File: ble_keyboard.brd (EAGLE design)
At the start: 52 x 23 mm, 18 parts, among them CN1 FH34SRJ-6S, CN2 FH34SRJ-10S, CON1 41002W90-NP-S-30, Q1 DMG6968U-7, U1 YJ-14015

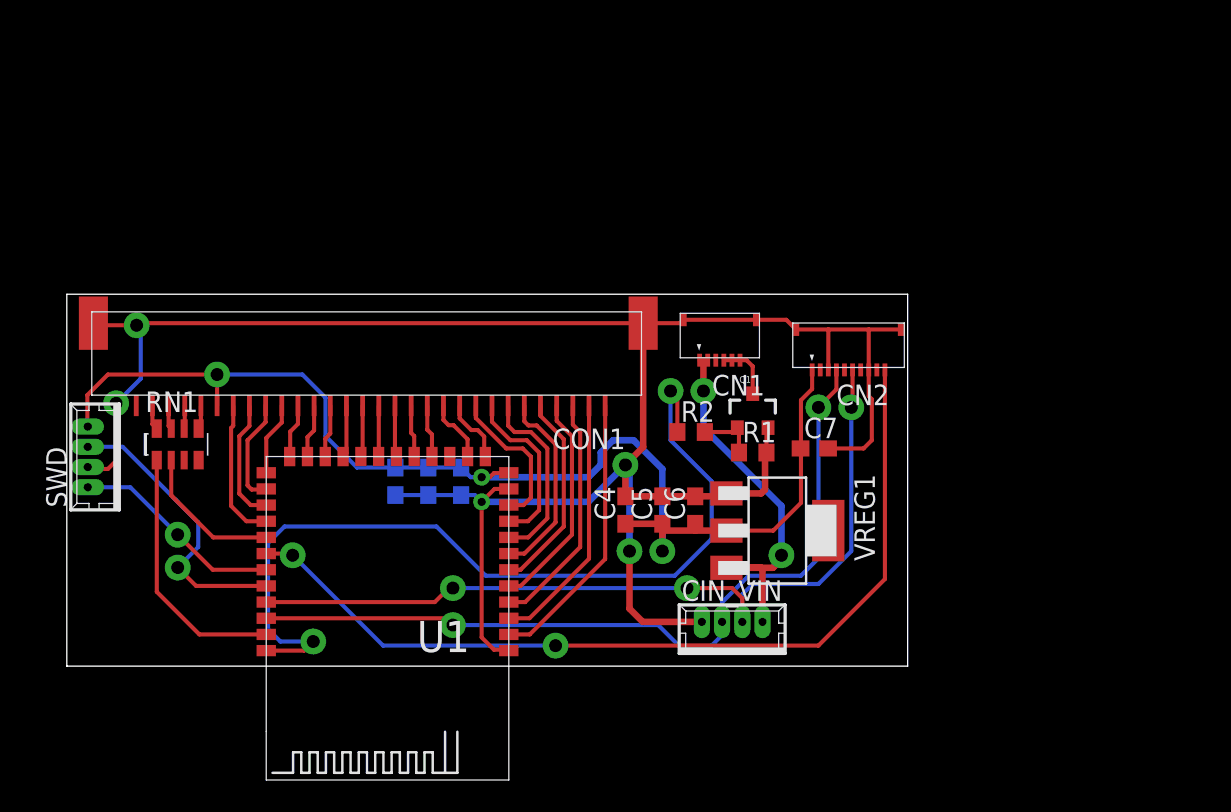
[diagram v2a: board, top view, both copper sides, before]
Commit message: Brd routed with 90 degree rotated BLE module, fixed touchpad and Keyboard pinout
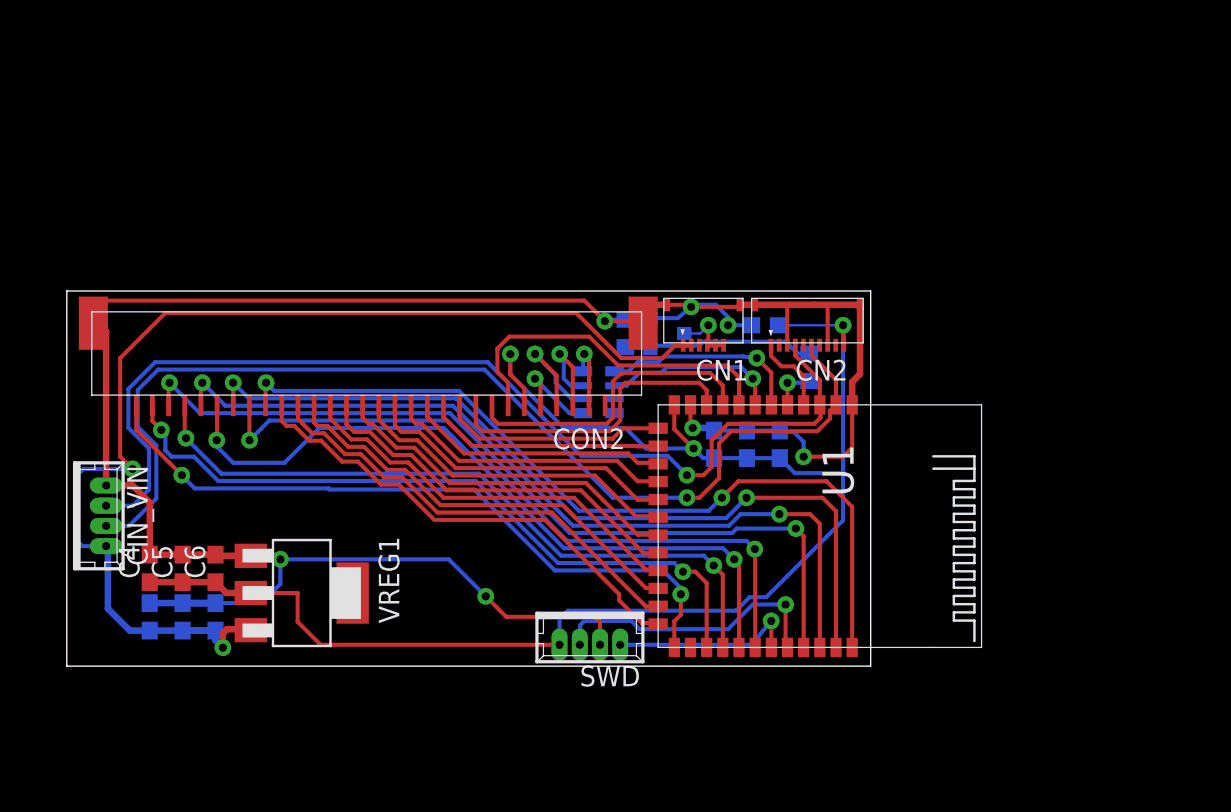
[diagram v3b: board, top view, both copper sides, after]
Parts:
- added C10: 1uF, rcl:C0603
- added C8: 10nF, rcl:C0603
- added C9: 100n, rcl:C0603
- moved CIN_VIN 39.8 mm to (1.98, 9.30), turned to 270 degrees
- moved SWD 32.6 mm to (32.4, 1.77), turned to 180 degrees
- moved C6 29.9 mm to (9.19, 6.05)
- moved C5 29.9 mm to (7.16, 6.05)
- moved VREG1 29.7 mm to (14.5, 4.52)
- moved C4 29.6 mm to (5.13, 6.05)
- moved RN1 26.2 mm to (32.9, 16.9), flipped to the bottom, turned to 270 degrees
- moved C3 23.9 mm to (44.1, 13.7), turned to 90 degrees
- moved C2 19.8 mm to (42.1, 13.7), turned to 90 degrees
- moved U1 17.3 mm to (36.6, 8.66), turned to 270 degrees
- moved C1 15.8 mm to (40.0, 13.7), turned to 90 degrees
- moved R1 10.8 mm to (34.5, 20.6), flipped to the bottom, turned to 90 degrees
- moved R2 8.33 mm to (45.9, 18.5), flipped to the bottom, turned to 90 degrees
- moved C7 8.21 mm to (43.2, 21.1), flipped to the bottom
- moved Q1 7.19 mm to (37.1, 20.6), flipped to the bottom, turned to 90 degrees
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- renumbered CON1 to CON2
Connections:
- net +3V3: now also CN2.10, CON2.6; no longer CN2.1, CON2.25
- net BACKLIGHT_PWM: now also U1.P.24; no longer U1.P.20
- net GND: now also C10.2, C8.2, C9.2
- net I2C_SCL: now also CIN_VIN.2, CN2.6, U1.P.21; no longer CIN_VIN.3, CN2.4, U1.P.18
- net I2C_SDA: now also CIN_VIN.3, CN2.4, U1.P.22; no longer CIN_VIN.2, CN2.6, U1.P.17
- net KSI0: now also CON2.25, U1.P.15; no longer CON2.5, U1.P.25
- net KSI1: now also CON2.23, U1.P.16; no longer CON2.7, U1.P.27
- net KSI2: now also CON2.24, U1.P.19; no longer CON2.8, U1.P.28
- net KSI3: now also CON2.22, U1.P.20; no longer CON2.9, U1.P.29
- net KSI4: now also CON2.21, U1.P.10; no longer CON2.10, U1.P.30
- net KSI5: now also CON2.19, U1.P.08; no longer CON2.12, U1.P.02
- net KSI6: now also CON2.17, U1.P.06; no longer CON2.14, U1.P.04
- net KSI7: now also CON2.16; no longer CON2.15
- net KSO0: now also CON2.30, U1.P.11; no longer CON2.1, U1.P.21
- net KSO1: now also CON2.29, U1.P.13; no longer CON2.2, U1.P.22
- net KSO10: now also CON2.12, U1.P.01; no longer CON2.19, U1.P.09
- net KSO11: now also CON2.11, U1.P.00; no longer CON2.20, U1.P.10
- net KSO12: now also CON2.10, U1.P.30; no longer CON2.21, U1.P.11
- net KSO13: now also CON2.9, U1.P.29; no longer CON2.22, U1.P.12
- net KSO14: now also CON2.8, U1.P.28; no longer CON2.23, U1.P.13
- net KSO15: now also CON2.7, U1.P.27; no longer CON2.24, U1.P.14
- net KSO2: now also CON2.27, U1.P.14; no longer CON2.3, U1.P.23
- net KSO3: now also CON2.28, U1.P.17; no longer CON2.4, U1.P.24
- net KSO4: now also CON2.26, U1.P.18; no longer CON2.6, U1.P.26
- net KSO5: now also CON2.20, U1.P.09; no longer CON2.11, U1.P.00
- net KSO6: now also CON2.18, U1.P.07; no longer CON2.13, U1.P.03
- net KSO7: now also CON2.15, U1.P.04; no longer CON2.16, U1.P.06
- net KSO8: now also CON2.14, U1.P.03; no longer CON2.17, U1.P.07
- net KSO9: now also CON2.13, U1.P.02; no longer CON2.18, U1.P.08
- net LED_CAPS: now also U1.P.26; no longer U1.P.15
- net LED_FN: now also U1.P.25; no longer U1.P.19
- net LIPO_RAW: now also C10.1, C8.1, C9.1
- net N$1: now also CON2.5; no longer CON2.26
- net N$2: now also CON2.4; no longer CON2.27
- net N$3: now also CON2.3; no longer CON2.28
- net N$4: now also CON2.2; no longer CON2.29
- net TOUCH_ALERT: now also CN2.1, U1.P.23; no longer CN2.10, U1.P.16
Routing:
- net BACKLIGHT_PWM: track 54.6 -> 2.75 mm, vias 2 -> 1
- net TOUCH_ALERT: track 55.3 -> 4.97 mm, vias 2 -> 0
- net LIPO_RAW: track 24.0 -> 72.0 mm
- net KSI3: track 9.26 -> 51.1 mm, vias 0 -> 2
- net KSI2: track 10.4 -> 51.5 mm, vias 0 -> 2
- net KSO4: track 12.0 -> 51.5 mm, vias 0 -> 2
- net KSO3: track 13.6 -> 51.7 mm, vias 0 -> 2
- net KSI0: track 12.6 -> 44.8 mm, vias 0 -> 2
- net KSI1: track 11.4 -> 43.3 mm, vias 0 -> 2
- net KSO2: track 14.8 -> 43.2 mm, vias 0 -> 2
- net KSO1: track 16.0 -> 44.0 mm, vias 0 -> 2
- net KSO0: track 17.4 -> 43.1 mm, vias 0 -> 2
- net KSI4: track 4.04 -> 29.7 mm
- net KSO5: track 3.94 -> 27.9 mm
- net +3V3: track 75.2 -> 99.0 mm
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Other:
- board size 52 x 23 mm -> 49.7 x 23.2 mm

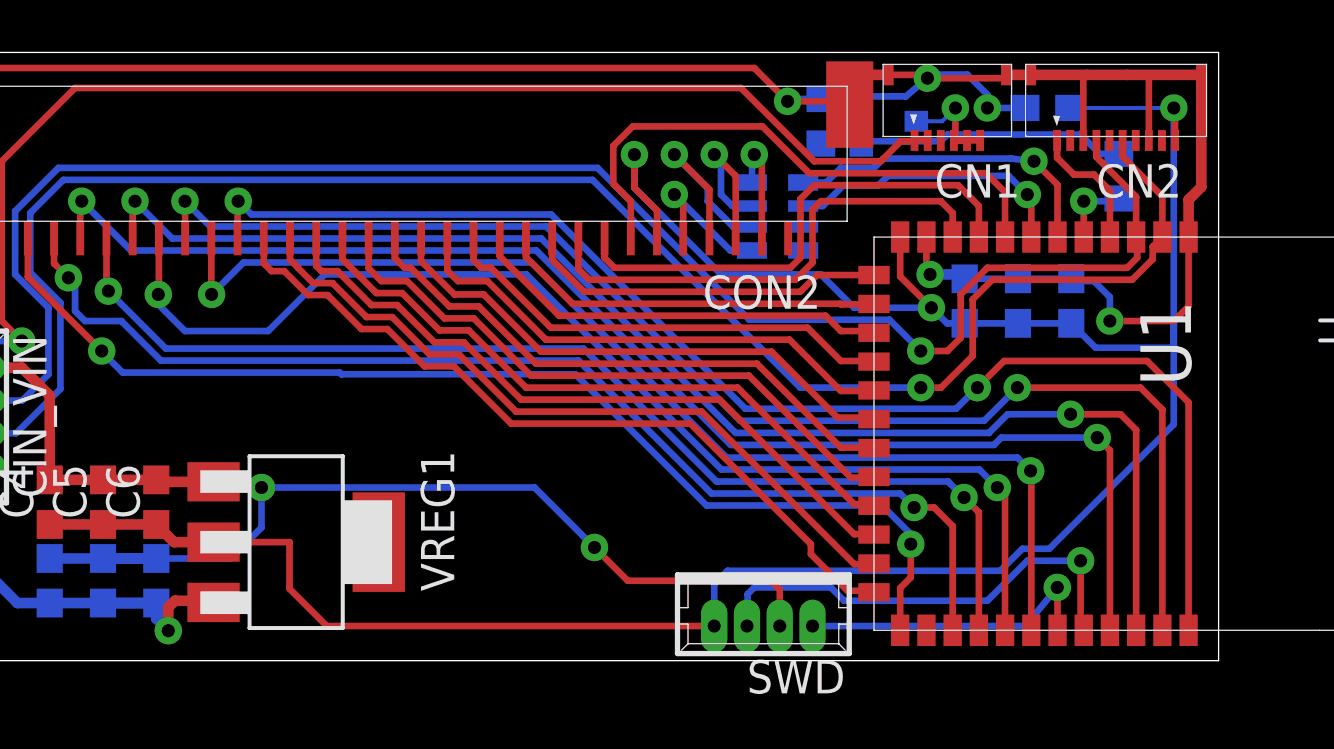
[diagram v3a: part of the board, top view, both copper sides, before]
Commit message: Cleaned up schematic mess, fixed keyboard BL pinout mirroring.
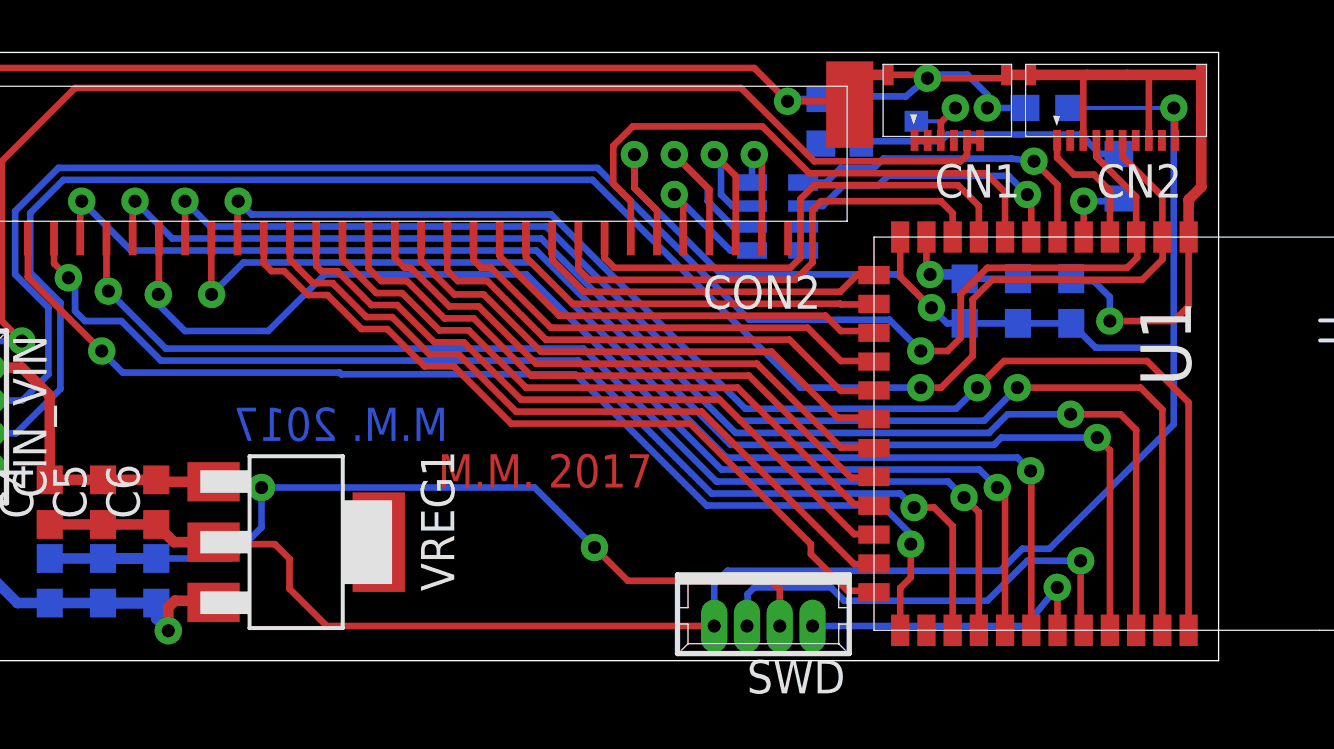
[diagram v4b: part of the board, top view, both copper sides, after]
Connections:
- net BACKL_LED_K: now also CN1.1, CN1.2, CN1.3; no longer CN1.4, CN1.5, CN1.6
- net KSI0: now also CON2.26, U1.P.18; no longer CON2.25, U1.P.15
- net KSI1: now also CON2.24, U1.P.19; no longer CON2.23, U1.P.16
- net KSI2: now also CON2.23, U1.P.16; no longer CON2.24, U1.P.19
- net KSO2: now also CON2.28, U1.P.17; no longer CON2.27, U1.P.14
- net KSO3: now also CON2.27, U1.P.14; no longer CON2.28, U1.P.17
- net KSO4: now also CON2.25, U1.P.15; no longer CON2.26, U1.P.18
- net LIPO_RAW: now also CN1.5, CN1.6; no longer CN1.1, CN1.2
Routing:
- net KSO3: track 51.7 -> 43.2 mm
- net KSO2: track 43.2 -> 51.7 mm
- net KSI2: track 51.5 -> 43.3 mm
- net KSI1: track 43.3 -> 51.5 mm
- net KSO4: track 51.5 -> 44.8 mm
- net KSI0: track 44.8 -> 51.5 mm
- net LIPO_RAW: track 72.0 -> 74.3 mm
- net +3V3: track 99.0 -> 97.7 mm
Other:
- board text added: "M.M. 2017"

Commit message: Sikscreen cleanup before Gerberization
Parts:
- renumbered CIN_VIN to CON3
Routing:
- net KSO4: track 44.8 -> 43.0 mm
- net KSI2: track 43.3 -> 42.3 mm
- net LED_CAPS: track 11.0 -> 10.4 mm
- net GND: vias 7 -> 11
- added copper zone on layer 1, net GND
- added copper zone on layer 16, net GND
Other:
- board text added: "C1"
- board text added: "C10"
- board text added: "C2"
- board text added: "C3"
- board text added: "C4"
- board text added: "C5"
- board text added: "C6"
- board text added: "C7"
- board text added: "C8"
- board text added: "C9"
- board text added: "CN1"
- board text added: "CN2"
- board text added: "CON2"
- board text added: "CON3"
- board text added: "Q1"
- board text added: "R1"
- board text added: "R2"
- board text added: "RN1"
- board text added: "U1"
- board text added: "VCC SWDCLK GND SWDIO"
- board text added: "VREG1"

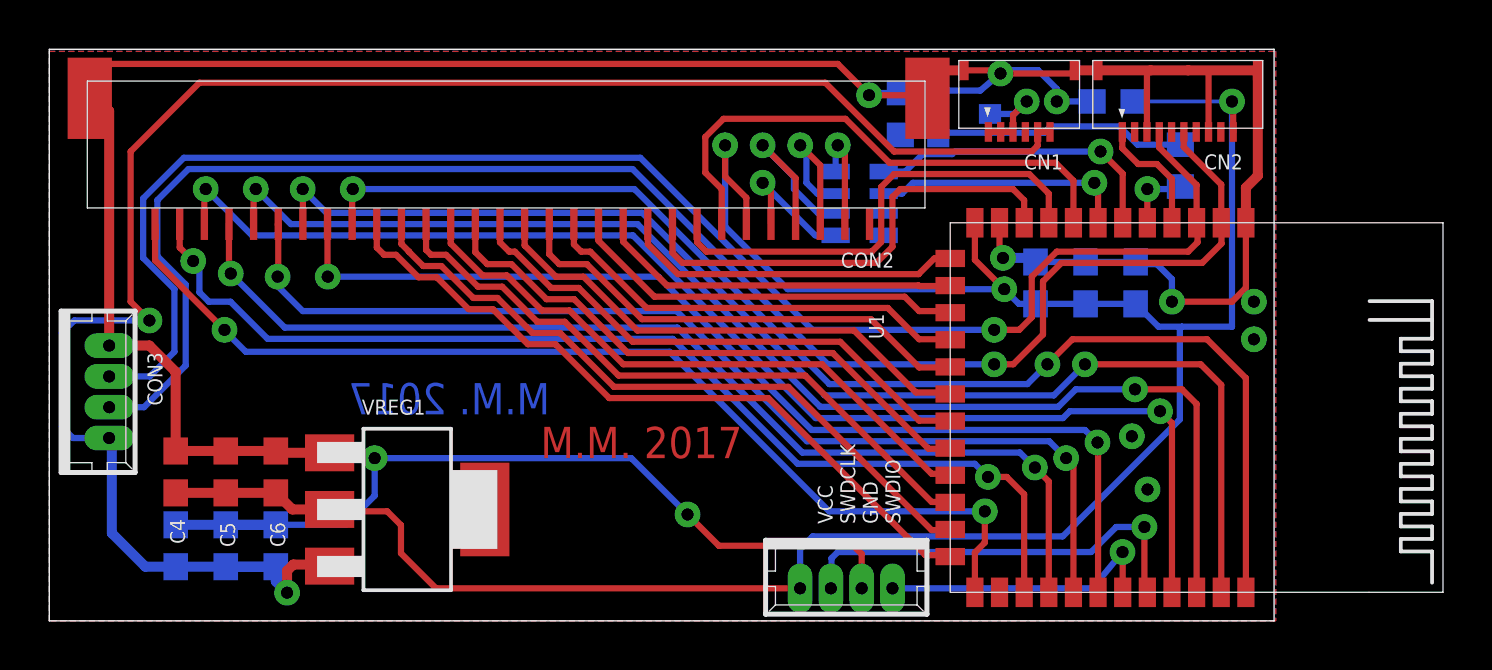
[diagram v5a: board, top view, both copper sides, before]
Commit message: Updated BT module footprint
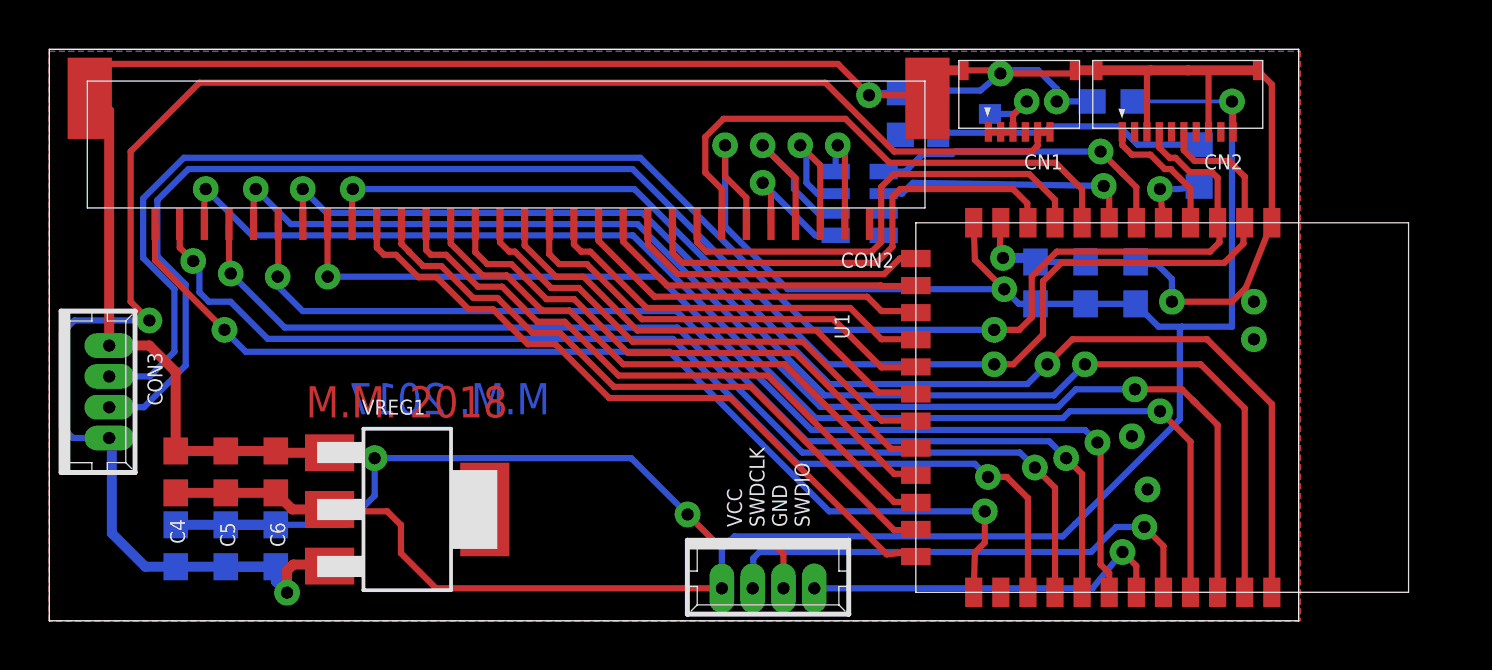
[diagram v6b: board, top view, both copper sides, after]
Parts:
- moved SWD 3.18 mm to (29.2, 1.77)
- moved U1 1.40 mm to (35.2, 8.66)
- moved R2 0.76 mm to (46.7, 18.5)
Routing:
- net SWDCLK: track 17.2 -> 20.6 mm
- net SWDIO: track 11.7 -> 15.1 mm
- net GND: track 148.3 -> 145.4 mm
- net I2C_SCL: track 66.5 -> 68.6 mm
- net I2C_SDA: track 63.8 -> 65.7 mm
- net KSO8: track 19.4 -> 18.0 mm
- net KSO7: track 20.6 -> 19.2 mm
- net KSO12: track 13.9 -> 12.5 mm
- net KSO10: track 16.2 -> 14.8 mm
- net KSO6: track 25.0 -> 23.7 mm
- net KSO5: track 27.9 -> 26.7 mm
- net KSI6: track 23.7 -> 22.5 mm
- net KSO9: track 17.7 -> 16.5 mm
- net KSI7: track 22.0 -> 20.8 mm
- net KSI5: track 26.6 -> 25.4 mm
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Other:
- board size 49.7 x 23.2 mm -> 50.7 x 23.2 mm
- board text added: "M.M. 2018"

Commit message: Schematic cleanup
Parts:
- added Q2: DMG2305UX-7, transistor-fet:SC75_INFINEON
- added R3: 47K, rcl:R0603
- RN1: value 2K -> 1K5
- VREG1: value MIC5200-3.3YS -> MCP1703T-3302E/DB
- renumbered CN1 to BACKLIGHT, CN2 to TOUCHPAD, CON2 to KEYBOARD, CON3 to PWR
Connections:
- net N$1 renamed LED_TP_R
- net N$2 renamed LED_RFOFF_R
- net N$3 renamed LED_CAPS_R
- net N$4 renamed LED_FN_R
- new net NENABLE_TOUCHPAD: Q2.1, R3.1, U1.P.12
- new net V_TOUCHPAD: Q2.2, TOUCHPAD.10
- net +3V3: now also Q2.3, R3.2; no longer TOUCHPAD.10
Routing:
- net NENABLE_TOUCHPAD: track 0.00 -> 26.2 mm, vias 0 -> 1
- net V_TOUCHPAD: track 0.00 -> 4.53 mm, vias 0 -> 1
- net SWDIO: track 15.1 -> 16.2 mm
- net GND: track 145.4 -> 146.4 mm, vias 11 -> 10
- net KSO0: track 42.9 -> 42.3 mm
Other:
- board text added: "GND SMBUS_SDA SMBUS_SCL VBAT"
- board text removed: "M.M. 2017"
